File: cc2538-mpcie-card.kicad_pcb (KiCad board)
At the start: 2 copper layers, 30.1 x 50.8 mm, 25 parts, among them J1 Bus_PCI_Express_Mini, J2 Conn_ARM_JTAG_SWD_10, Q1 MUN5214DW1, Q2 MUN5214DW1, U1 CC2538_SZ12, U2 CP2102N-A01-GQFN24

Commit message: Reworked USB, added power LED & cap
The USB conection used to have dangling stubs, due to the likely
unpopulated direct connection to the CC2538 native USB. It has now been
reworked to use 0402 components, and the series resistor now rests
directly on the vias, minimizing the amount of stub. Although it's just
low speed USB, I doubt it would affect much.

Additionally, wired up the activity LED (PB4) to the system's WLAN
indicator, and added a power LED (PB1), which would be turned on by the
module to indicate it's alive.

Also added a capacitor near the module's 3V3 connection.
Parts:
- removed R4: 33R, Resistor_SMD:R_0603_1608Metric
- added C8: 1uF, Capacitor_SMD:C_0603_1608Metric, F.Cu at (133.8, 124.5)
- added D1: LED_Small, LED_SMD:LED_0603_1608Metric, F.Cu at (133.6, 137.4)
- added RN3: 33R, Resistor_SMD:R_Array_Convex_2x0402, B.Cu at (152.5, 145.9)
- C4, C5: footprint Capacitor_SMD:C_0603_1608Metric -> Capacitor_SMD:C_0402_1005Metric
- R2: footprint Resistor_SMD:R_0603_1608Metric -> Resistor_SMD:R_0402_1005Metric; moved to F.Cu
- R3: value 33R -> 1K; moved to F.Cu
- moved R3 19.4 mm to (133.6, 140.4)
- moved R2 7.80 mm to (150.4, 146.3)
- moved TP2 3.22 mm to (143.4, 141.9)
- moved C5 3.02 mm to (152.4, 143.8), turned to 0 degrees
- moved C4 2.59 mm to (154.2, 144.8), turned to 0 degrees
- moved TP1 2.24 mm to (146.6, 142.0)
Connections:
- R3 pad 1: /CC_USB+ -> Net-(D1-Pad2)
- R3 pad 2: /USB+ -> +3V3
- U1 pad 12: (no net) -> /~LED_PWR
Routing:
- net /USB+: track 17.0 -> 7.04 mm
- net /USB_FS_PU: track 2.48 -> 7.72 mm, vias 1 -> 2
- net /USB-: track 9.88 -> 5.55 mm
- net GND: track 38.7 -> 42.8 mm, vias 16 -> 20
- net Net-(J1-Pad30): track 9.69 -> 12.7 mm
- net Net-(J1-Pad32): track 12.4 -> 9.85 mm
- net /CC_USB+: track 19.1 -> 21.7 mm
- net /~LED_PWR: track 0.00 -> 2.21 mm
- net /CC_USB-: track 18.4 -> 20.4 mm
- net +3V3: track 77.0 -> 78.8 mm, vias 7 -> 8
- net Net-(D1-Pad2): track 0.00 -> 1.39 mm

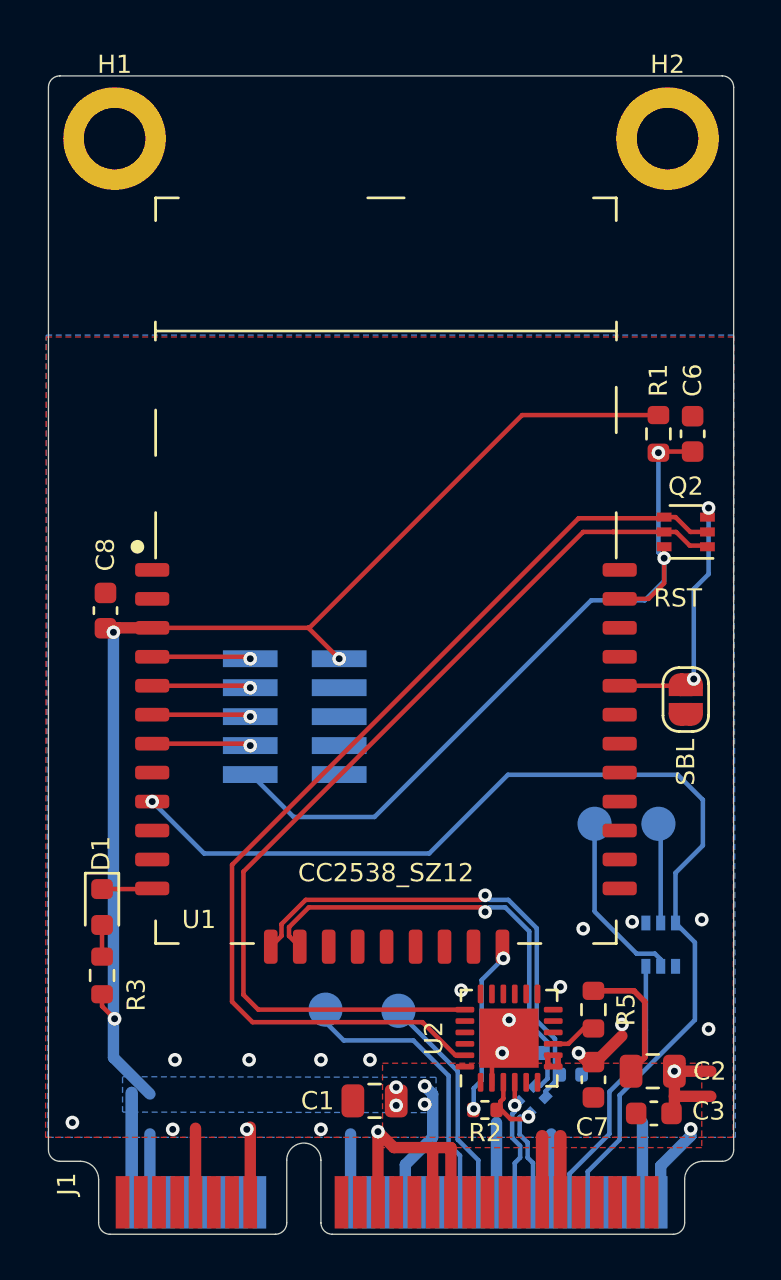
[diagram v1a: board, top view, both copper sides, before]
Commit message: Added PCB markings & text
- Labelled pinout for JTAG connector
- Added PCB "title" & date
- Added PCB manufacturer number marker
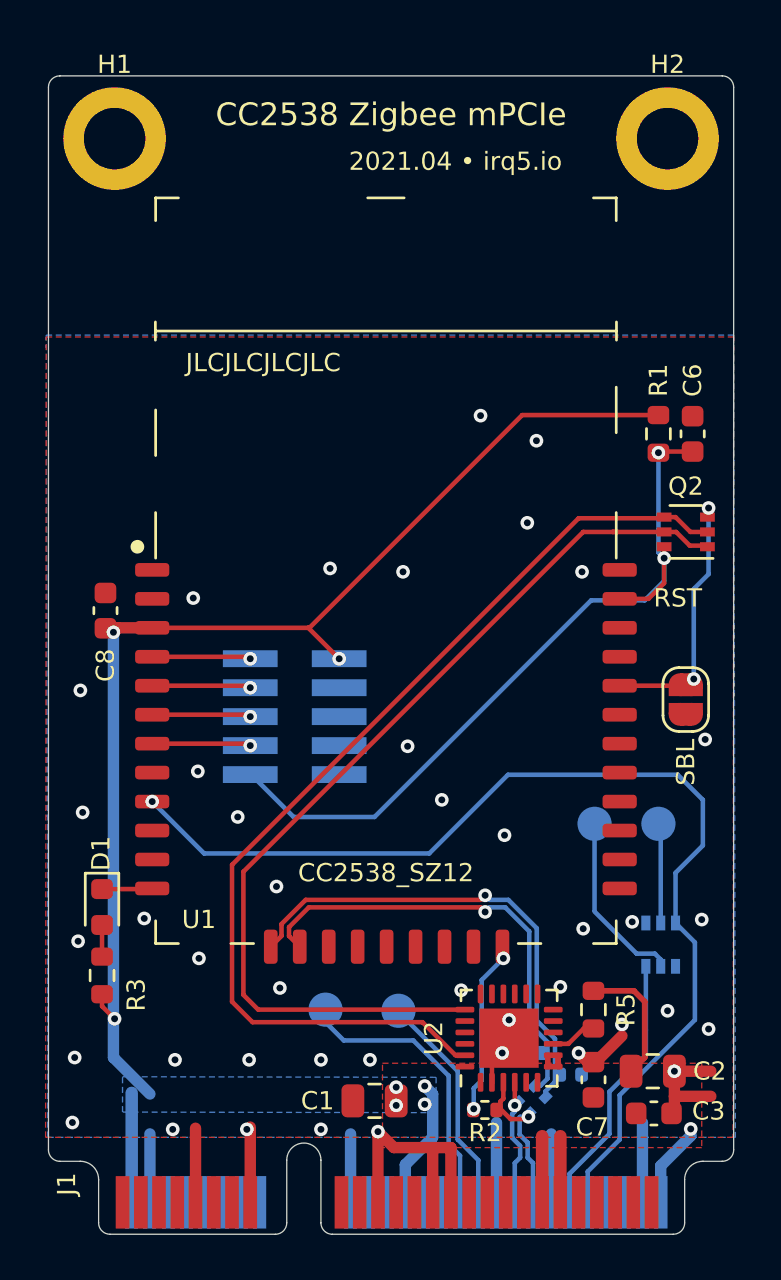
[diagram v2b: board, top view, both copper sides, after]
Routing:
- net GND: vias 20 -> 42
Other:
- board text added: "2021.04 • irq5.io"
- board text added: "CC2538 Zigbee mPCIe"
- board text added: "GND"
- board text added: "JLCJLCJLCJLC"
- board text added: "TCK"
- board text added: "TDI"
- board text added: "TDO"
- board text added: "TMS"
- board text added: "Vref"
- board text added: "~RST"
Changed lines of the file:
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@@
   (general
     (thickness 1.6)
-    (drawings 27)
-    (tracks 256)
+    (drawings 37)
+    (tracks 278)
     (zones 0)
     (modules 27)
@@
     (tags capacitor)
     (attr smd)
-    (fp_text reference C8 (at -2.45 0 90) (layer F.SilkS)
+    (fp_text reference C8 (at 2.4 0 90) (layer F.SilkS)
       (effects (font (size 0.8 0.8) (thickness 0.1)))
     )
@@
     (tags "Surface mounted pin header SMD 2x05 1.27mm double row")
     (attr smd)
-    (fp_text reference J2 (at 0 4.235) (layer B.SilkS)
+    (fp_text reference J2 (at 0 4.235) (layer B.SilkS) hide
       (effects (font (size 0.8 0.8) (thickness 0.1)) (justify mirror))
     )
@@
       (rotate (xyz 0 0 0))
     )
+    (fp_text user JTAG (at -0.01 4 180) (layer B.SilkS)
+      (effects (font (size 0.8 0.8) (thickness 0.1)) (justify mirror))
+    )
   )
   (module Capacitor_SMD:C_0603_1608Metric (layer F.Cu)
@@
       (rotate (xyz 0 0 0))
     )
+  )
+  (gr_text JLCJLCJLCJLC (at 140.67 113.58) (layer F.SilkS)
+    (effects (font (size 0.8 0.8) (thickness 0.1)))
+  )
+  (gr_text TDI (at 138.561905 130.33275) (layer B.SilkS)
+    (effects (font (size 0.8 0.8) (thickness 0.1)) (justify left mirror))
+  )
+  (gr_text ~RST (at 138.561905 131.71) (layer B.SilkS)
+    (effects (font (size 0.8 0.8) (thickness 0.1)) (justify left mirror))
+  )
+  (gr_text TDO (at 138.561905 129.0585) (layer B.SilkS)
+    (effects (font (size 0.8 0.8) (thickness 0.1)) (justify left mirror))
+  )
+  (gr_text TCK (at 138.561905 127.78425) (layer B.SilkS)
+    (effects (font (size 0.8 0.8) (thickness 0.1)) (justify left mirror))
+  )
+  (gr_text TMS (at 138.561905 126.51) (layer B.SilkS)
+    (effects (font (size 0.8 0.8) (thickness 0.1)) (justify left mirror))
+  )
+  (gr_text GND (at 145.58 127.89) (layer B.SilkS)
+    (effects (font (size 0.8 0.8) (thickness 0.1)) (justify right mirror))
+  )
+  (gr_text Vref (at 145.58 126.58) (layer B.SilkS)
+    (effects (font (size 0.8 0.8) (thickness 0.1)) (justify right mirror))
+  )
+  (gr_text "2021.04 • irq5.io" (at 149.1 104.75) (layer F.SilkS)
+    (effects (font (size 0.8 0.8) (thickness 0.1)))
+  )
+  (gr_text "CC2538 Zigbee mPCIe" (at 146.275 102.7) (layer F.SilkS)
+    (effects (font (size 1 1) (thickness 0.15)))
   )
   (gr_text RST (at 158.85 123.9) (layer F.SilkS)
@@
   (segment (start 158.7 144.65) (end 158.7 146.375) (width 0.5) (layer F.Cu) (net 1))
   (segment (start 158.7 145.75) (end 160.3 145.75) (width 0.5) (layer F.Cu) (net 1))
-  (segment (start 153.1 143.85) (end 152.82 143.85) (width 0.2) (layer B.Cu) (net 21))
+  (via (at 143.6 122.6) (size 0.6) (drill 0.3) (layers F.Cu B.Cu) (net 1))
+  (via (at 146.8 122.75) (size 0.6) (drill 0.3) (layers F.Cu B.Cu) (net 1))
+  (via (at 150.2 115.9) (size 0.6) (drill 0.3) (layers F.Cu B.Cu) (net 1))
+  (via (at 152.65 117) (size 0.6) (drill 0.3) (layers F.Cu B.Cu) (net 1))
+  (via (at 152.25 120.6) (size 0.6) (drill 0.3) (layers F.Cu B.Cu) (net 1))
+  (via (at 154.65 122.75) (size 0.6) (drill 0.3) (layers F.Cu B.Cu) (net 1))
+  (via (at 147 130.4) (size 0.6) (drill 0.3) (layers F.Cu B.Cu) (net 1))
+  (via (at 148.5 132.75) (size 0.6) (drill 0.3) (layers F.Cu B.Cu) (net 1))
+  (via (at 151.25 134.3) (size 0.6) (drill 0.3) (layers F.Cu B.Cu) (net 1))
+  (via (at 141.25 136.55) (size 0.6) (drill 0.3) (layers F.Cu B.Cu) (net 1))
+  (via (at 139.55 133.5) (size 0.6) (drill 0.3) (layers F.Cu B.Cu) (net 1))
+  (via (at 137.85 139.7) (size 0.6) (drill 0.3) (layers F.Cu B.Cu) (net 1))
+  (via (at 141.4 141) (size 0.6) (drill 0.3) (layers F.Cu B.Cu) (net 1))
+  (via (at 158.4 142) (size 0.6) (drill 0.3) (layers F.Cu B.Cu) (net 1))
+  (via (at 160.05 130.1) (size 0.6) (drill 0.3) (layers F.Cu B.Cu) (net 1))
+  (via (at 132.65 127.95) (size 0.6) (drill 0.3) (layers F.Cu B.Cu) (net 1))
+  (via (at 137.6 123.9) (size 0.6) (drill 0.3) (layers F.Cu B.Cu) (net 1))
+  (via (at 137.8 131.5) (size 0.6) (drill 0.3) (layers F.Cu B.Cu) (net 1))
+  (via (at 132.75 133.3) (size 0.6) (drill 0.3) (layers F.Cu B.Cu) (net 1))
+  (via (at 135.45 137.95) (size 0.6) (drill 0.3) (layers F.Cu B.Cu) (net 1))
+  (via (at 132.55 138.95) (size 0.6) (drill 0.3) (layers F.Cu B.Cu) (net 1))
+  (via (at 132.4 144.05) (size 0.6) (drill 0.3) (layers F.Cu B.Cu) (net 1))
   (segment (start 149.3 150.4) (end 149.3 148.35) (width 0.2) (layer B.Cu) (net 2) (status 10))
   (segment (start 149.3 148.35) (end 148.8 147.85) (width 0.2) (layer B.Cu) (net 2))
@@
   (segment (start 152.665 138.381654) (end 152.665 142.431654) (width 0.2) (layer B.Cu) (net 20))
   (segment (start 153.465 145.113321) (end 153.465 143.231654) (width 0.2) (layer B.Cu) (net 20))
+  (segment (start 153.75 144.8) (end 153.47 144.8) (width 0.2) (layer B.Cu) (net 20))
+  (segment (start 153.1 143.85) (end 152.82 143.85) (width 0.2) (layer B.Cu) (net 21))
   (segment (start 152.818736 145.292893) (end 153.135 144.976629) (width 0.2) (layer B.Cu) (net 21) (status 10))
   (segment (start 152.557107 145.292893) (end 152.818736 145.292893) (width 0.2) (layer B.Cu) (net 21) (status 30))
@@
   (segment (start 152.93 143.9) (end 153 143.9) (width 0.2) (layer B.Cu) (net 21) (status 30))
   (segment (start 153.135 144.976629) (end 153.135 143.368346) (width 0.2) (layer B.Cu) (net 21))
-  (segment (start 153.75 144.8) (end 153.47 144.8) (width 0.2) (layer B.Cu) (net 20))
   (segment (start 158.75 138.15) (end 158.75 135.95) (width 0.2) (layer B.Cu) (net 22) (status 10))
   (segment (start 158.75 135.95) (end 159.95 134.75) (width 0.2) (layer B.Cu) (net 22))

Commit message: Added PCB dimension markings
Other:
- board text added: "PCB thickness: 1.00mm"
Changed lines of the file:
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@@
   (general
     (thickness 1.6)
-    (drawings 37)
+    (drawings 40)
     (tracks 278)
     (zones 0)
@@
     )
   )
+  (gr_text "PCB thickness: 1.00mm" (at 146.275 153.24) (layer Dwgs.User)
+    (effects (font (size 1 1) (thickness 0.15)))
+  )
+  (dimension 30.05 (width 0.15) (layer Dwgs.User)
+    (gr_text "30.050 mm" (at 146.275 98.5) (layer Dwgs.User)
+      (effects (font (size 1 1) (thickness 0.15)))
+    )
+    (feature1 (pts (xy 161.3 101.5) (xy 161.3 99.213579)))
+    (feature2 (pts (xy 131.25 101.5) (xy 131.25 99.213579)))
+    (crossbar (pts (xy 131.25 99.8) (xy 161.3 99.8)))
+    (arrow1a (pts (xy 161.3 99.8) (xy 160.173496 100.386421)))
+    (arrow1b (pts (xy 161.3 99.8) (xy 160.173496 99.213579)))
+    (arrow2a (pts (xy 131.25 99.8) (xy 132.376504 100.386421)))
+    (arrow2b (pts (xy 131.25 99.8) (xy 132.376504 99.213579)))
+  )
+  (dimension 50.8 (width 0.15) (layer Dwgs.User)
+    (gr_text "50.800 mm" (at 128.250001 126.4 270) (layer Dwgs.User)
+      (effects (font (size 1 1) (thickness 0.15)))
+    )
+    (feature1 (pts (xy 131.75 151.8) (xy 128.96358 151.8)))
+    (feature2 (pts (xy 131.75 101) (xy 128.96358 101)))
+    (crossbar (pts (xy 129.550001 101) (xy 129.550001 151.8)))
+    (arrow1a (pts (xy 129.550001 151.8) (xy 128.96358 150.673496)))
+    (arrow1b (pts (xy 129.550001 151.8) (xy 130.136422 150.673496)))
+    (arrow2a (pts (xy 129.550001 101) (xy 128.96358 102.126504)))
+    (arrow2b (pts (xy 129.550001 101) (xy 130.136422 102.126504)))
+  )
   (gr_text JLCJLCJLCJLC (at 140.67 113.58) (layer F.SilkS)
